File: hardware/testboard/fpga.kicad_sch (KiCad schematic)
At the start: 42 parts, among them J2 Conn_01x06, SW1 Button, U10 SN74ALVC164245, U11 ICE40HX4K-TQ144, U12 74AHCT04, U13 SST26VF023BA, U18 SN74LVC07, U19 SN74LVC07

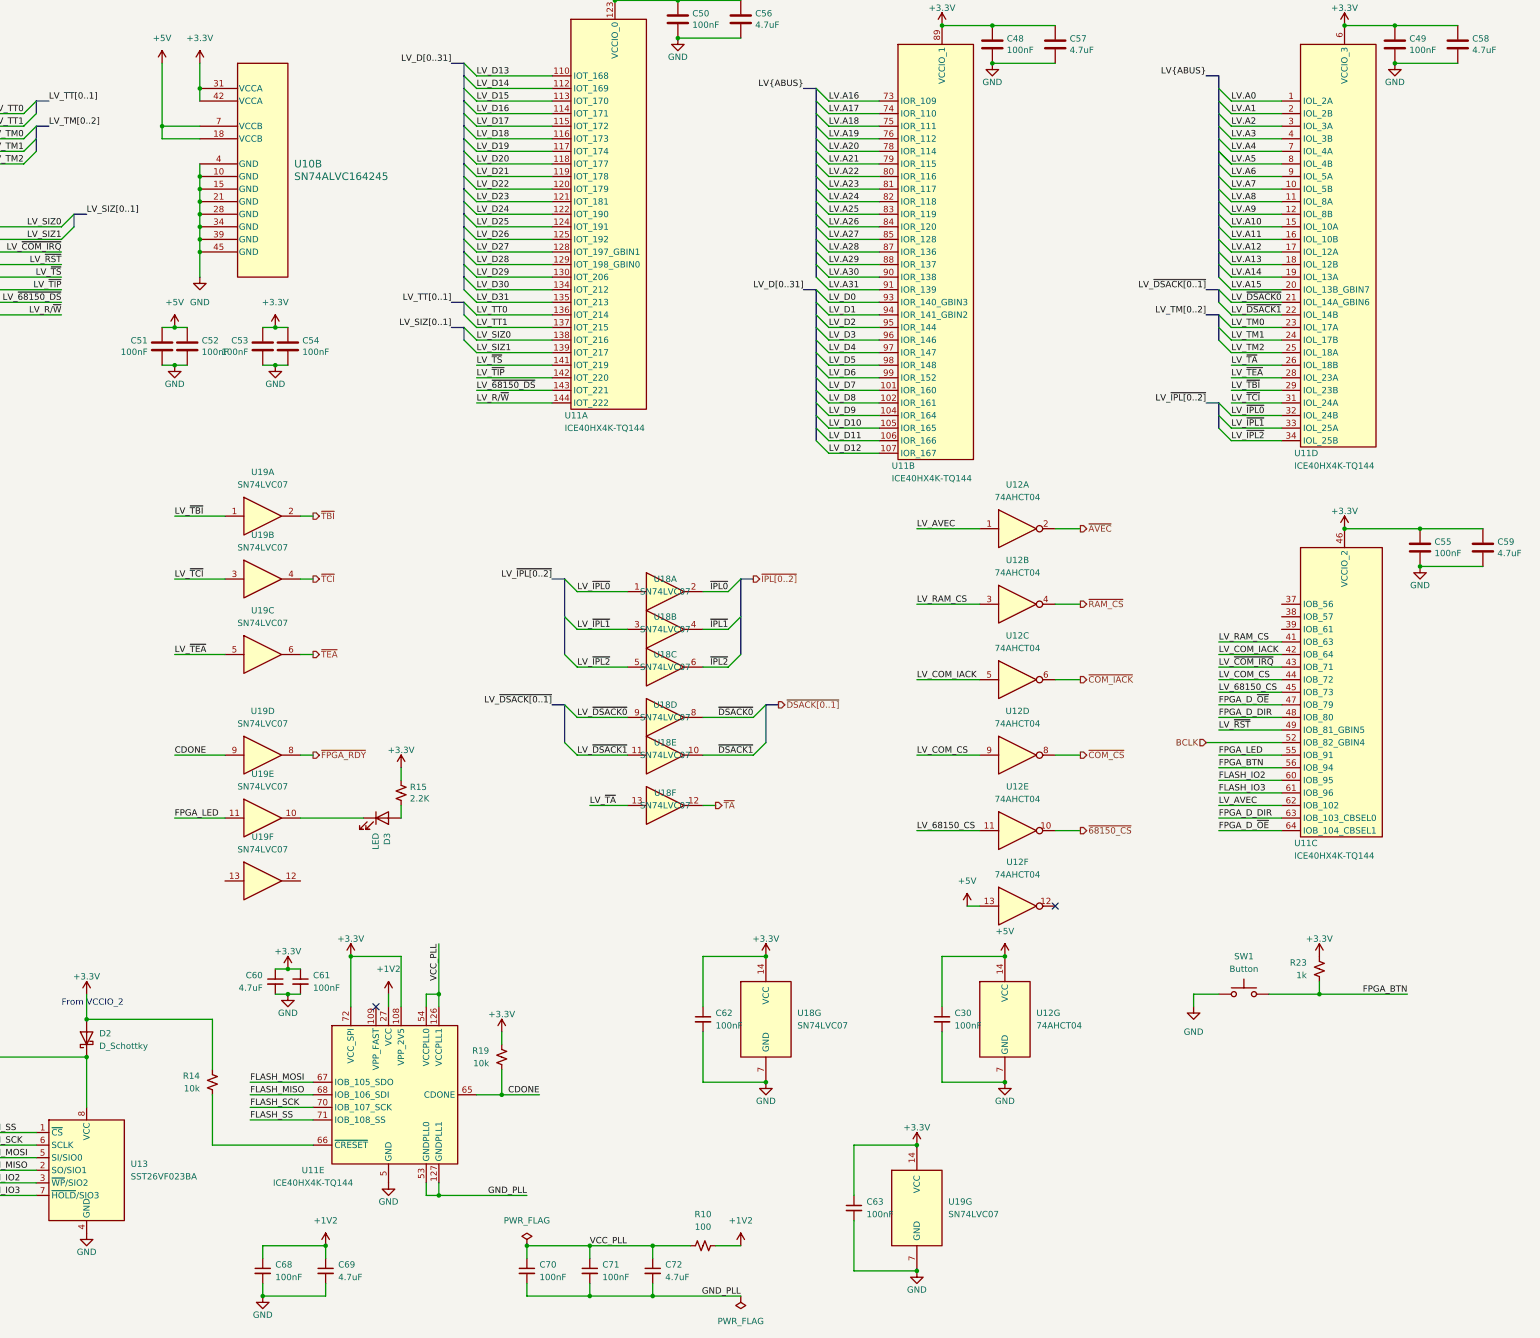
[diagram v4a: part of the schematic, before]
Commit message: fix up FPGA pinning
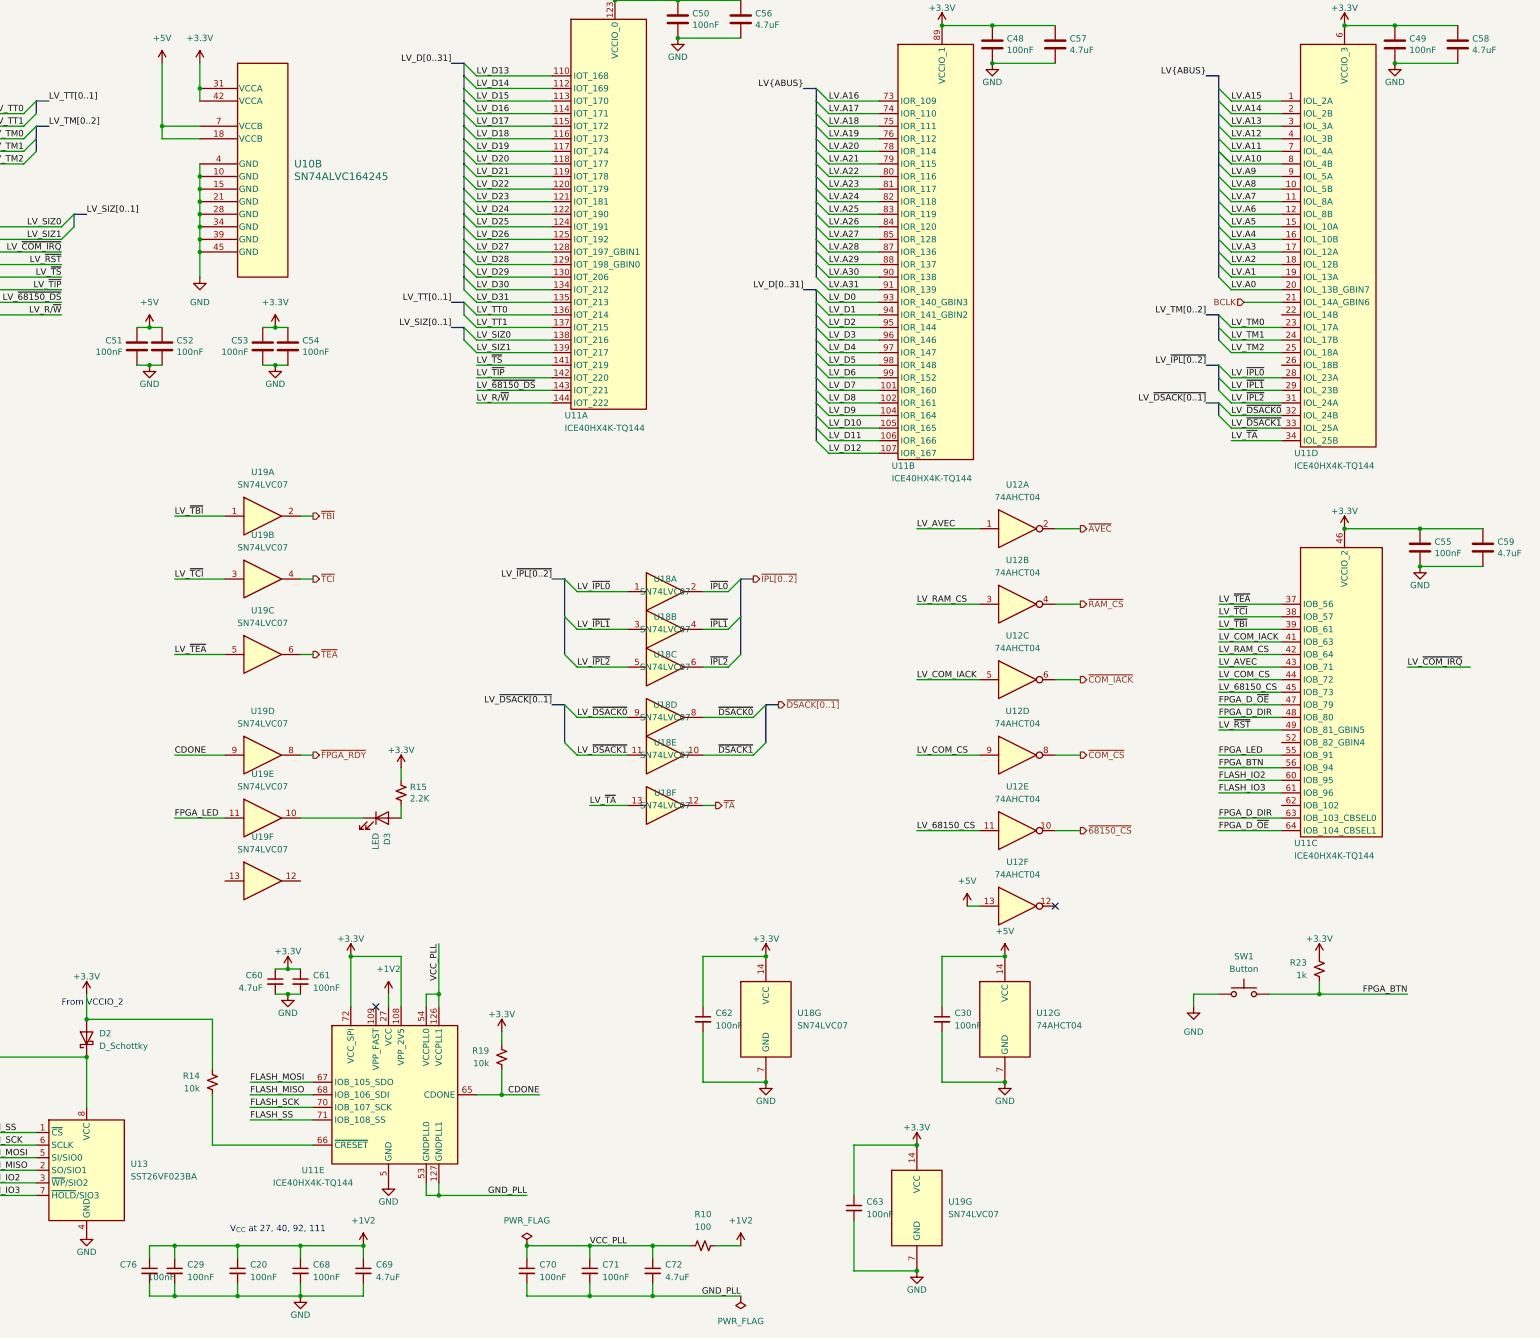
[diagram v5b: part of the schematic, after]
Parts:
- added C20, C29, C76: 100nF, Capacitor_SMD:C_0603_1608Metric, symbol Device:C_Small
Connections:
- net +1V2: now also C20.1, C29.1, C76.1
- net BCLK: now also U11.21 (IOL_14A_GBIN6); no longer U11.52 (IOB_82_GBIN4)
- net GND: now also C20.2, C29.2, C76.2
- net LV.A0: now also U11.20 (IOL_13B_GBIN7); no longer U11.1 (IOL_2A)
- net LV.A1: now also U11.19 (IOL_13A); no longer U11.2 (IOL_2B)
- net LV.A10: now also U11.8 (IOL_4B); no longer U11.15 (IOL_10A)
- net LV.A11: now also U11.7 (IOL_4A); no longer U11.16 (IOL_10B)
- net LV.A12: now also U11.4 (IOL_3B); no longer U11.17 (IOL_12A)
- net LV.A13: now also U11.3 (IOL_3A); no longer U11.18 (IOL_12B)
- net LV.A14: now also U11.2 (IOL_2B); no longer U11.19 (IOL_13A)
- net LV.A15: now also U11.1 (IOL_2A); no longer U11.20 (IOL_13B_GBIN7)
- net LV.A2: now also U11.18 (IOL_12B); no longer U11.3 (IOL_3A)
- net LV.A3: now also U11.17 (IOL_12A); no longer U11.4 (IOL_3B)
- net LV.A4: now also U11.16 (IOL_10B); no longer U11.7 (IOL_4A)
- net LV.A5: now also U11.15 (IOL_10A); no longer U11.8 (IOL_4B)
- net LV.A6: now also U11.12 (IOL_8B); no longer U11.9 (IOL_5A)
- net LV.A7: now also U11.11 (IOL_8A); no longer U11.10 (IOL_5B)
- net LV.A8: now also U11.10 (IOL_5B); no longer U11.11 (IOL_8A)
- net LV.A9: now also U11.9 (IOL_5A); no longer U11.12 (IOL_8B)
- net LV_AVEC: now also U11.43 (IOB_71); no longer U11.62 (IOB_102)
- net LV_COM_IACK: now also U11.41 (IOB_63); no longer U11.42 (IOB_64)
- net LV_RAM_CS: now also U11.42 (IOB_64); no longer U11.41 (IOB_63)
- net LV_~{COM_IRQ}: no longer U11.43 (IOB_71)
- net LV_~{DSACK0}: now also U11.32 (IOL_24B); no longer U11.21 (IOL_14A_GBIN6)
- net LV_~{DSACK1}: now also U11.33 (IOL_25A); no longer U11.22 (IOL_14B)
- net LV_~{IPL0}: now also U11.28 (IOL_23A); no longer U11.32 (IOL_24B)
- net LV_~{IPL1}: now also U11.29 (IOL_23B); no longer U11.33 (IOL_25A)
- net LV_~{IPL2}: now also U11.31 (IOL_24A); no longer U11.34 (IOL_25B)
- net LV_~{TA}: now also U11.34 (IOL_25B); no longer U11.26 (IOL_18B)
- net LV_~{TBI}: now also U11.39 (IOB_61); no longer U11.29 (IOL_23B)
- net LV_~{TCI}: now also U11.38 (IOB_57); no longer U11.31 (IOL_24A)
- net LV_~{TEA}: now also U11.37 (IOB_56); no longer U11.28 (IOL_23A)
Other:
- note added: "V_{CC} at 27, 40, 92, 111"
- moved on the sheet: C51, C52, C68, C69

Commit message: I ripped it all apart
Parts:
- added C? (x16): 100nF, Capacitor_SMD:C_0603_1608Metric, symbol Device:C
- added R?: R_Small_US, Resistor_SMD:R_0603_1608Metric, symbol Device:R_Small_US
- added U? (x8): SN74ALVC164245, Package_SO:TSSOP-48_6.1x12.5mm_P0.5mm, symbol 68040:SN74ALVC164245
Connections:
- net +3.3V: now also C?.1, C?.1, C?.1, C?.1, C?.1, C?.1, C?.1, C?.1, R?.1, U?.31 (VCCA), U?.31 (VCCA), U?.31 (VCCA), U?.31 (VCCA), U?.42 (VCCA), U?.42 (VCCA), U?.42 (VCCA), U?.42 (VCCA)
- net +5V: now also C?.1, C?.1, C?.1, C?.1, C?.1, C?.1, C?.1, C?.1, U?.18 (VCCB), U?.18 (VCCB), U?.18 (VCCB), U?.18 (VCCB), U?.7 (VCCB), U?.7 (VCCB), U?.7 (VCCB), U?.7 (VCCB)
- net BCLK: no longer U11.21 (IOL_14A_GBIN6)
- net FLASH_IO2: no longer U11.60 (IOB_95)
- net FLASH_IO3: no longer U11.61 (IOB_96)
- net FPGA_BTN: no longer U11.56 (IOB_94)
- net FPGA_D_DIR: no longer U11.48 (IOB_80), U11.63 (IOB_103_CBSEL0)
- net FPGA_D_~{OE}: no longer U11.47 (IOB_79), U11.64 (IOB_104_CBSEL1)
- net FPGA_LED: no longer U11.55 (IOB_91)
- net GND: now also C?.2, C?.2, C?.2, C?.2, C?.2, C?.2, C?.2, C?.2, C?.2, C?.2, C?.2, C?.2, C?.2, C?.2, C?.2, C?.2, U?.1 (1DIR), U?.1 (1DIR), U?.10 (GND), U?.10 (GND), U?.10 (GND), U?.10 (GND), U?.15 (GND), U?.15 (GND), U?.15 (GND), U?.15 (GND), U?.21 (GND), U?.21 (GND), U?.21 (GND), U?.21 (GND), U?.24 (2DIR), U?.24 (2DIR), U?.25 (*2OE), U?.25 (*2OE), U?.28 (GND), U?.28 (GND), U?.28 (GND), U?.28 (GND), U?.34 (GND), U?.34 (GND), U?.34 (GND), U?.34 (GND), U?.39 (GND), U?.39 (GND), U?.39 (GND), U?.39 (GND), U?.4 (GND), U?.4 (GND), U?.4 (GND), U?.4 (GND), U?.45 (GND), U?.45 (GND), U?.45 (GND), U?.45 (GND), U?.48 (*1OE), U?.48 (*1OE); no longer U10.11 (1B7), U10.12 (1B8), U10.9 (1B6)
- net LV.A0: now also U?.47 (1A1); no longer U11.20 (IOL_13B_GBIN7)
- net LV.A1: now also U?.46 (1A2); no longer U11.19 (IOL_13A)
- net LV.A10: now also U?.33 (2A3); no longer U11.8 (IOL_4B)
- net LV.A11: now also U?.32 (2A4); no longer U11.7 (IOL_4A)
- net LV.A12: now also U?.30 (2A5); no longer U11.4 (IOL_3B)
- net LV.A13: now also U?.29 (2A6); no longer U11.3 (IOL_3A)
- net LV.A14: now also U?.27 (2A7); no longer U11.2 (IOL_2B)
- net LV.A15: now also U?.26 (2A8); no longer U11.1 (IOL_2A)
- net LV.A16: now also U?.47 (1A1); no longer U11.73 (IOR_109)
- net LV.A17: now also U?.46 (1A2); no longer U11.74 (IOR_110)
- net LV.A18: now also U?.44 (1A3); no longer U11.75 (IOR_111)
- net LV.A19: now also U?.43 (1A4); no longer U11.76 (IOR_112)
- net LV.A2: now also U?.44 (1A3); no longer U11.18 (IOL_12B)
- net LV.A20: now also U?.41 (1A5); no longer U11.78 (IOR_114)
- net LV.A21: now also U?.40 (1A6); no longer U11.79 (IOR_115)
- net LV.A22: now also U?.38 (1A7); no longer U11.80 (IOR_116)
- net LV.A23: now also U?.37 (1A8); no longer U11.81 (IOR_117)
- net LV.A24: now also U?.36 (2A1); no longer U11.82 (IOR_118)
- net LV.A25: now also U?.35 (2A2); no longer U11.83 (IOR_119)
- net LV.A26: now also U?.33 (2A3); no longer U11.84 (IOR_120)
- net LV.A27: now also U?.32 (2A4); no longer U11.85 (IOR_128)
- net LV.A28: now also U?.30 (2A5); no longer U11.87 (IOR_136)
- net LV.A29: now also U?.29 (2A6); no longer U11.88 (IOR_137)
- net LV.A3: now also U?.43 (1A4); no longer U11.17 (IOL_12A)
- net LV.A30: now also U?.27 (2A7); no longer U11.90 (IOR_138)
- net LV.A31: now also U?.26 (2A8); no longer U11.91 (IOR_139)
- net LV.A4: now also U?.41 (1A5); no longer U11.16 (IOL_10B)
- net LV.A5: now also U?.40 (1A6); no longer U11.15 (IOL_10A)
- net LV.A6: now also U?.38 (1A7); no longer U11.12 (IOL_8B)
- net LV.A7: now also U?.37 (1A8); no longer U11.11 (IOL_8A)
- net LV.A8: now also U?.36 (2A1); no longer U11.10 (IOL_5B)
- net LV.A9: now also U?.35 (2A2); no longer U11.9 (IOL_5A)
- net LV_68150_CS: no longer U11.45 (IOB_73)
- net LV_AVEC: no longer U11.43 (IOB_71)
- net LV_COM_CS: no longer U11.44 (IOB_72)
- net LV_COM_IACK: no longer U11.41 (IOB_63)
- net LV_D0: now also U?.47 (1A1); no longer U11.93 (IOR_140_GBIN3)
- net LV_D1: now also U?.46 (1A2); no longer U11.94 (IOR_141_GBIN2)
- net LV_D10: now also U?.33 (2A3); no longer U11.105 (IOR_165)
- net LV_D11: now also U?.32 (2A4); no longer U11.106 (IOR_166)
- net LV_D12: now also U?.30 (2A5); no longer U11.107 (IOR_167)
- net LV_D13: now also U?.29 (2A6); no longer U11.110 (IOT_168)
- net LV_D14: now also U?.27 (2A7); no longer U11.112 (IOT_169)
- net LV_D15: now also U?.26 (2A8); no longer U11.113 (IOT_170)
- net LV_D16: now also U?.47 (1A1); no longer U11.114 (IOT_171)
- net LV_D17: now also U?.46 (1A2); no longer U11.115 (IOT_172)
- net LV_D18: now also U?.44 (1A3); no longer U11.116 (IOT_173)
- net LV_D19: now also U?.43 (1A4); no longer U11.117 (IOT_174)
- net LV_D2: now also U?.44 (1A3); no longer U11.95 (IOR_144)
- net LV_D20: now also U?.41 (1A5); no longer U11.118 (IOT_177)
- net LV_D21: now also U?.40 (1A6); no longer U11.119 (IOT_178)
- net LV_D22: now also U?.38 (1A7); no longer U11.120 (IOT_179)
- net LV_D23: now also U?.37 (1A8); no longer U11.121 (IOT_181)
- net LV_D24: now also U?.36 (2A1); no longer U11.122 (IOT_190)
- net LV_D25: now also U?.35 (2A2); no longer U11.124 (IOT_191)
- net LV_D26: now also U?.33 (2A3); no longer U11.125 (IOT_192)
- net LV_D27: now also U?.32 (2A4); no longer U11.128 (IOT_197_GBIN1)
- net LV_D28: now also U?.30 (2A5); no longer U11.129 (IOT_198_GBIN0)
- net LV_D29: now also U?.29 (2A6); no longer U11.130 (IOT_206)
- net LV_D3: now also U?.43 (1A4); no longer U11.96 (IOR_146)
- net LV_D30: now also U?.27 (2A7); no longer U11.134 (IOT_212)
- net LV_D31: now also U?.26 (2A8); no longer U11.135 (IOT_213)
- net LV_D4: now also U?.41 (1A5); no longer U11.97 (IOR_147)
- net LV_D5: now also U?.40 (1A6); no longer U11.98 (IOR_148)
- net LV_D6: now also U?.38 (1A7); no longer U11.99 (IOR_152)
- net LV_D7: now also U?.37 (1A8); no longer U11.101 (IOR_160)
- net LV_D8: now also U?.36 (2A1); no longer U11.102 (IOR_161)
- net LV_D9: now also U?.35 (2A2); no longer U11.104 (IOR_164)
- net LV_RAM_CS: no longer U11.42 (IOB_64)
- net LV_R/~{W}: no longer U10.26 (2A8), U11.144 (IOT_222)
- net LV_SIZ0: no longer U10.36 (2A1), U11.138 (IOT_216)
- net LV_SIZ1: no longer U10.35 (2A2), U11.139 (IOT_217)
- net LV_TM0: no longer U10.44 (1A3), U11.23 (IOL_17A)
- net LV_TM1: no longer U10.43 (1A4), U11.24 (IOL_17B)
- net LV_TM2: no longer U10.41 (1A5), U11.25 (IOL_18A)
- net LV_TT0: no longer U10.47 (1A1), U11.136 (IOT_214)
- net LV_TT1: no longer U10.46 (1A2), U11.137 (IOT_215)
- net LV_~{68150_DS}: no longer U10.27 (2A7), U11.143 (IOT_221)
- net LV_~{COM_IRQ}: no longer U10.33 (2A3)
- net LV_~{DSACK0}: no longer U11.32 (IOL_24B)
- net LV_~{DSACK1}: no longer U11.33 (IOL_25A)
- net LV_~{IPL0}: no longer U11.28 (IOL_23A)
- net LV_~{IPL1}: no longer U11.29 (IOL_23B)
- net LV_~{IPL2}: no longer U11.31 (IOL_24A)
- net LV_~{RST}: no longer U10.32 (2A4), U11.49 (IOB_81_GBIN5)
- net LV_~{TA}: no longer U11.34 (IOL_25B)
- net LV_~{TBI}: no longer U11.39 (IOB_61)
- net LV_~{TCI}: no longer U11.38 (IOB_57)
- net LV_~{TEA}: no longer U11.37 (IOB_56)
- net LV_~{TIP}: no longer U10.29 (2A6), U11.142 (IOT_220)
- net LV_~{TS}: no longer U10.30 (2A5), U11.141 (IOT_219)
- net R/~{W}: now also U10.13 (2B1); no longer U10.23 (2B8)
- net SIZ0: now also U10.12 (1B8); no longer U10.13 (2B1)
- net SIZ1: now also U10.11 (1B7); no longer U10.14 (2B2)
- net TM0: now also U10.9 (1B6); no longer U10.5 (1B3)
- net TM1: now also U10.8 (1B5); no longer U10.6 (1B4)
- net TM2: now also U10.6 (1B4); no longer U10.8 (1B5)
- net TT0: now also U10.5 (1B3); no longer U10.2 (1B1)
- net ~{68150_DS}: now also U10.2 (1B1); no longer U10.22 (2B7)
- net ~{RST}: now also U10.19 (2B5); no longer U10.17 (2B4)
- net ~{TS}: now also U10.22 (2B7); no longer U10.19 (2B5)
- new net A0: U?.2 (1B1)
- new net A1: U?.3 (1B2)
- new net A10: U?.16 (2B3)
- new net A11: U?.17 (2B4)
- new net A12: U?.19 (2B5)
- new net A13: U?.20 (2B6)
- new net A14: U?.22 (2B7)
- new net A15: U?.23 (2B8)
- new net A16: U?.2 (1B1)
- new net A17: U?.3 (1B2)
- new net A18: U?.5 (1B3)
- new net A19: U?.6 (1B4)
- new net A2: U?.5 (1B3)
- new net A20: U?.8 (1B5)
- new net A21: U?.9 (1B6)
- new net A22: U?.11 (1B7)
- new net A23: U?.12 (1B8)
- new net A24: U?.13 (2B1)
- new net A25: U?.14 (2B2)
- new net A26: U?.16 (2B3)
- new net A27: U?.17 (2B4)
- new net A28: U?.19 (2B5)
- new net A29: U?.20 (2B6)
- new net A3: U?.6 (1B4)
- new net A30: U?.22 (2B7)
- new net A31: U?.23 (2B8)
- new net A4: U?.8 (1B5)
- new net A5: U?.9 (1B6)
- new net A6: U?.11 (1B7)
- new net A7: U?.12 (1B8)
- new net A8: U?.13 (2B1)
- new net A9: U?.14 (2B2)
- new net D0: U?.2 (1B1)
- new net D1: U?.3 (1B2)
- new net D10: U?.16 (2B3)
- new net D11: U?.17 (2B4)
- new net D12: U?.19 (2B5)
- new net D13: U?.20 (2B6)
- new net D14: U?.22 (2B7)
- new net D15: U?.23 (2B8)
- new net D16: U?.2 (1B1)
- new net D17: U?.3 (1B2)
- new net D18: U?.5 (1B3)
- new net D19: U?.6 (1B4)
- new net D2: U?.5 (1B3)
- new net D20: U?.8 (1B5)
- new net D21: U?.9 (1B6)
- new net D22: U?.11 (1B7)
- new net D23: U?.12 (1B8)
- new net D24: U?.13 (2B1)
- new net D25: U?.14 (2B2)
- new net D26: U?.16 (2B3)
- new net D27: U?.17 (2B4)
- new net D28: U?.19 (2B5)
- new net D29: U?.20 (2B6)
- new net D3: U?.6 (1B4)
- new net D30: U?.22 (2B7)
- new net D31: U?.23 (2B8)
- new net D4: U?.8 (1B5)
- new net D5: U?.9 (1B6)
- new net D6: U?.11 (1B7)
- new net D7: U?.12 (1B8)
- new net D8: U?.13 (2B1)
- new net D9: U?.14 (2B2)
- new net FPGA_DBUF_DIR: U?.1 (1DIR), U?.1 (1DIR), U?.24 (2DIR), U?.24 (2DIR)
- new net FPGA_DBUF_~{OE}: R?.2, U?.25 (*2OE), U?.25 (*2OE), U?.48 (*1OE), U?.48 (*1OE)
- no-connect marks 5 -> 2
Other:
- removed sheet AddressBuffer
- removed sheet DataTRX
- moved on the sheet: C20, C29, C30, C31, C48, C49, C50, C51, C52, C53, C54, C55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

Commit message: pinouts
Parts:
- gave numbers to parts that had none: 21
- renumbered C31 to C801, C51 to C802, C52 to C803, C76 to C804, C53 to C805, C29 to C806, C54 to C807, C20 to C808, C60 to C809, C61 to C810, C68 to C811, C69 to C812, C70 to C813, C71 to C814, C72 to C815, C50 to C816, C56 to C821, C48 to C834, C57 to C835, C62 to C836, C30 to C837, C49 to C838, C58 to C839, C63 to C840, C55 to C841, C59 to C842, D1 to D801, D2 to D802, D3 to D803, J2 to J801, R16 to R801, R23 to R802, R17 to R803, R18 to R804, R14 to R805, R19 to R806, R10 to R808, R15 to R809, SW1 to SW801, U13 to U801, U10 to U802, U11 to U803, U18 to U808, U12 to U809, U19 to U810
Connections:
- net A0: now also U805.23 (2B8); no longer U806.2 (1B1)
- net A1: now also U805.22 (2B7); no longer U806.3 (1B2)
- net A10: now also U806.2 (1B1); no longer U806.16 (2B3)
- net A11: now also U806.3 (1B2); no longer U806.17 (2B4)
- net A12: now also U806.5 (1B3); no longer U806.19 (2B5)
- net A13: now also U806.6 (1B4); no longer U806.20 (2B6)
- net A14: now also U806.8 (1B5); no longer U806.22 (2B7)
- net A15: now also U806.11 (1B7); no longer U806.23 (2B8)
- net A16: now also U806.9 (1B6); no longer U807.2 (1B1)
- net A17: now also U806.12 (1B8); no longer U807.3 (1B2)
- net A18: now also U806.14 (2B2); no longer U807.5 (1B3)
- net A19: now also U806.13 (2B1); no longer U807.6 (1B4)
- net A2: now also U805.20 (2B6); no longer U806.5 (1B3)
- net A20: now also U806.17 (2B4); no longer U807.8 (1B5)
- net A21: now also U806.20 (2B6); no longer U807.9 (1B6)
- net A22: now also U807.12 (1B8); no longer U807.11 (1B7)
- net A23: now also U806.16 (2B3); no longer U807.12 (1B8)
- net A24: now also U807.8 (1B5); no longer U807.13 (2B1)
- net A25: now also U806.19 (2B5); no longer U807.14 (2B2)
- net A26: now also U807.11 (1B7); no longer U807.16 (2B3)
- net A27: now also U807.5 (1B3); no longer U807.17 (2B4)
- net A28: now also U807.9 (1B6); no longer U807.19 (2B5)
- net A29: now also U807.3 (1B2); no longer U807.20 (2B6)
- net A3: now also U805.19 (2B5); no longer U806.6 (1B4)
- net A30: now also U807.6 (1B4); no longer U807.22 (2B7)
- net A31: now also U807.2 (1B1); no longer U807.23 (2B8)
- net A4: now also U805.17 (2B4); no longer U806.8 (1B5)
- net A5: now also U805.16 (2B3); no longer U806.9 (1B6)
- net A6: now also U805.14 (2B2); no longer U806.11 (1B7)
- net A7: now also U805.13 (2B1); no longer U806.12 (1B8)
- net A8: now also U806.23 (2B8); no longer U806.13 (2B1)
- net A9: now also U806.22 (2B7); no longer U806.14 (2B2)
- net BCLK: now also U803.94 (IOR_141_GBIN2)
- net D0: now also U807.13 (2B1); no longer U804.2 (1B1)
- net D1: now also U807.14 (2B2); no longer U804.3 (1B2)
- net D10: now also U804.5 (1B3); no longer U804.16 (2B3)
- net D11: now also U804.6 (1B4); no longer U804.17 (2B4)
- net D12: now also U804.8 (1B5); no longer U804.19 (2B5)
- net D13: now also U804.11 (1B7); no longer U804.20 (2B6)
- net D14: now also U804.13 (2B1); no longer U804.22 (2B7)
- net D15: now also U804.14 (2B2); no longer U804.23 (2B8)
- net D16: now also U804.9 (1B6); no longer U805.2 (1B1)
- net D17: now also U804.16 (2B3); no longer U805.3 (1B2)
- net D18: now also U804.12 (1B8); no longer U805.5 (1B3)
- net D19: now also U804.19 (2B5); no longer U805.6 (1B4)
- net D2: now also U807.17 (2B4); no longer U804.5 (1B3)
- net D20: now also U804.22 (2B7); no longer U805.8 (1B5)
- net D21: now also U805.2 (1B1); no longer U805.9 (1B6)
- net D22: now also U804.20 (2B6); no longer U805.11 (1B7)
- net D23: now also U804.17 (2B4); no longer U805.12 (1B8)
- net D24: now also U805.3 (1B2); no longer U805.13 (2B1)
- net D25: now also U804.23 (2B8); no longer U805.14 (2B2)
- net D26: now also U805.5 (1B3); no longer U805.16 (2B3)
- net D27: now also U805.8 (1B5); no longer U805.17 (2B4)
- net D28: now also U805.6 (1B4); no longer U805.19 (2B5)
- net D29: now also U805.11 (1B7); no longer U805.20 (2B6)
- net D3: now also U807.16 (2B3); no longer U804.6 (1B4)
- net D30: now also U805.12 (1B8); no longer U805.22 (2B7)
- net D31: now also U805.9 (1B6); no longer U805.23 (2B8)
- net D4: now also U807.19 (2B5); no longer U804.8 (1B5)
- net D5: now also U807.20 (2B6); no longer U804.9 (1B6)
- net D6: now also U807.22 (2B7); no longer U804.11 (1B7)
- net D7: now also U807.23 (2B8); no longer U804.12 (1B8)
- net D8: now also U804.2 (1B1); no longer U804.13 (2B1)
- net D9: now also U804.3 (1B2); no longer U804.14 (2B2)
- net FLASH_IO2: now also U803.56 (IOB_94)
- net FLASH_IO3: now also U803.60 (IOB_95)
- net FPGA_BTN: now also U803.55 (IOB_91)
- net FPGA_DBUF_DIR: no longer U805.24 (2DIR)
- net FPGA_DBUF_~{OE}: no longer U805.25 (*2OE)
- net FPGA_D_DIR: now also U803.47 (IOB_79), U803.62 (IOB_102)
- net FPGA_D_~{OE}: now also U803.45 (IOB_73), U803.63 (IOB_103_CBSEL0)
- net FPGA_LED: now also U803.52 (IOB_82_GBIN4)
- net GND: no longer U807.24 (2DIR), U807.25 (*2OE)
- net LV.A0: now also U803.37 (IOB_56), U805.26 (2A8); no longer U806.47 (1A1)
- net LV.A1: now also U803.34 (IOL_25B), U805.27 (2A7); no longer U806.46 (1A2)
- net LV.A10: now also U803.23 (IOL_17A), U806.47 (1A1); no longer U806.33 (2A3)
- net LV.A11: now also U803.22 (IOL_14B), U806.46 (1A2); no longer U806.32 (2A4)
- net LV.A12: now also U803.21 (IOL_14A_GBIN6), U806.44 (1A3); no longer U806.30 (2A5)
- net LV.A13: now also U803.20 (IOL_13B_GBIN7), U806.43 (1A4); no longer U806.29 (2A6)
- net LV.A14: now also U803.19 (IOL_13A), U806.41 (1A5); no longer U806.27 (2A7)
- net LV.A15: now also U803.18 (IOL_12B), U806.38 (1A7); no longer U806.26 (2A8)
- net LV.A16: now also U803.73 (IOR_109), U806.40 (1A6); no longer U807.47 (1A1)
- net LV.A17: now also U803.74 (IOR_110), U806.37 (1A8); no longer U807.46 (1A2)
- net LV.A18: now also U803.75 (IOR_111), U806.35 (2A2); no longer U807.44 (1A3)
- net LV.A19: now also U803.76 (IOR_112), U806.36 (2A1); no longer U807.43 (1A4)
- net LV.A2: now also U803.33 (IOL_25A), U805.29 (2A6); no longer U806.44 (1A3)
- net LV.A20: now also U803.78 (IOR_114), U806.32 (2A4); no longer U807.41 (1A5)
- net LV.A21: now also U803.79 (IOR_115), U806.29 (2A6); no longer U807.40 (1A6)
- net LV.A22: now also U803.80 (IOR_116), U807.37 (1A8); no longer U807.38 (1A7)
- net LV.A23: now also U803.81 (IOR_117), U806.33 (2A3); no longer U807.37 (1A8)
- net LV.A24: now also U803.82 (IOR_118), U807.41 (1A5); no longer U807.36 (2A1)
- net LV.A25: now also U803.83 (IOR_119), U806.30 (2A5); no longer U807.35 (2A2)
- net LV.A26: now also U803.84 (IOR_120), U807.38 (1A7); no longer U807.33 (2A3)
- net LV.A27: now also U803.85 (IOR_128), U807.44 (1A3); no longer U807.32 (2A4)
- net LV.A28: now also U803.87 (IOR_136), U807.40 (1A6); no longer U807.30 (2A5)
- net LV.A29: now also U803.88 (IOR_137), U807.46 (1A2); no longer U807.29 (2A6)
- net LV.A3: now also U803.32 (IOL_24B), U805.30 (2A5); no longer U806.43 (1A4)
- net LV.A30: now also U803.90 (IOR_138), U807.43 (1A4); no longer U807.27 (2A7)
- net LV.A31: now also U803.91 (IOR_139), U807.47 (1A1); no longer U807.26 (2A8)
- net LV.A4: now also U803.31 (IOL_24A), U805.32 (2A4); no longer U806.41 (1A5)
- net LV.A5: now also U803.29 (IOL_23B), U805.33 (2A3); no longer U806.40 (1A6)
- net LV.A6: now also U803.28 (IOL_23A), U805.35 (2A2); no longer U806.38 (1A7)
- net LV.A7: now also U803.26 (IOL_18B), U805.36 (2A1); no longer U806.37 (1A8)
- net LV.A8: now also U803.25 (IOL_18A), U806.26 (2A8); no longer U806.36 (2A1)
- net LV.A9: now also U803.24 (IOL_17B), U806.27 (2A7); no longer U806.35 (2A2)
- net LV_68150_CS: now also U803.44 (IOB_72)
- net LV_AVEC: now also U803.42 (IOB_64)
- net LV_COM_CS: now also U803.43 (IOB_71)
- net LV_COM_IACK: now also U803.39 (IOB_61)
- net LV_D0: now also U803.102 (IOR_161), U807.36 (2A1)
- net LV_D1: now also U803.104 (IOR_164), U807.35 (2A2)
- net LV_D10: now also U803.116 (IOT_173)
- net LV_D11: now also U803.117 (IOT_174)
- net LV_D12: now also U803.118 (IOT_177)
- net LV_D13: now also U803.119 (IOT_178)
- net LV_D14: now also U803.120 (IOT_179)
- net LV_D15: now also U803.121 (IOT_181)
- net LV_D16: now also U803.1 (IOL_2A)
- net LV_D17: now also U803.144 (IOT_222)
- net LV_D18: now also U803.143 (IOT_221)
- net LV_D19: now also U803.142 (IOT_220)
- net LV_D2: now also U803.105 (IOR_165), U807.32 (2A4)
- net LV_D20: now also U803.141 (IOT_219)
- net LV_D21: now also U803.139 (IOT_217)
- net LV_D22: now also U803.138 (IOT_216)
- net LV_D23: now also U803.137 (IOT_215)
- net LV_D24: now also U803.136 (IOT_214); no longer U805.36 (2A1)
- net LV_D25: now also U803.135 (IOT_213); no longer U805.35 (2A2)
- net LV_D26: now also U803.134 (IOT_212); no longer U805.33 (2A3)
- net LV_D27: now also U803.130 (IOT_206); no longer U805.32 (2A4)
- net LV_D28: now also U803.129 (IOT_198_GBIN0); no longer U805.30 (2A5)
- net LV_D29: now also U803.128 (IOT_197_GBIN1); no longer U805.29 (2A6)
- net LV_D3: now also U803.106 (IOR_166), U807.33 (2A3)
- net LV_D30: now also U803.125 (IOT_192); no longer U805.27 (2A7)
- net LV_D31: now also U803.124 (IOT_191); no longer U805.26 (2A8)
- net LV_D4: now also U803.107 (IOR_167), U807.30 (2A5)
- net LV_D5: now also U803.110 (IOT_168), U807.29 (2A6)
- net LV_D6: now also U803.112 (IOT_169), U807.27 (2A7)
- net LV_D7: now also U803.113 (IOT_170), U807.26 (2A8)
- net LV_D8: now also U803.114 (IOT_171)
- net LV_D9: now also U803.115 (IOT_172)
- net LV_RAM_CS: now also U803.41 (IOB_63)
- net LV_R/~{W}: now also U802.43 (1A4), U803.122 (IOT_190)
- net LV_SIZ0: now also U802.41 (1A5), U803.96 (IOR_146)
- net LV_SIZ1: now also U802.40 (1A6), U803.97 (IOR_147)
- net LV_TM0: now also U802.44 (1A3), U803.8 (IOL_4B)
- net LV_TM1: now also U802.46 (1A2), U803.9 (IOL_5A)
- net LV_TM2: now also U802.47 (1A1), U803.10 (IOL_5B)
- net LV_TT0: now also U803.93 (IOR_140_GBIN3)
- net LV_TT1: now also U803.95 (IOR_144)
- net LV_~{68150_DS}: now also U803.101 (IOR_160)
- net LV_~{COM_IRQ}: now also U803.64 (IOB_104_CBSEL1)
- net LV_~{DSACK0}: now also U803.11 (IOL_8A)
- net LV_~{DSACK1}: now also U803.12 (IOL_8B)
- net LV_~{IPL0}: now also U803.2 (IOL_2B)
- net LV_~{IPL1}: now also U803.3 (IOL_3A)
- net LV_~{IPL2}: now also U803.4 (IOL_3B)
- net LV_~{RST}: now also U803.48 (IOB_80)
- net LV_~{TA}: now also U803.7 (IOL_4A)
- net LV_~{TBI}: now also U803.17 (IOL_12A)
- net LV_~{TCI}: now also U803.16 (IOL_10B)
- net LV_~{TEA}: now also U803.15 (IOL_10A)
- net LV_~{TIP}: now also U802.37 (1A8), U803.99 (IOR_152)
- net LV_~{TS}: now also U802.38 (1A7), U803.98 (IOR_148)
- net R/~{W}: now also U802.6 (1B4); no longer U802.13 (2B1)
- net SIZ0: now also U802.8 (1B5); no longer U802.12 (1B8)
- net SIZ1: now also U802.9 (1B6); no longer U802.11 (1B7)
- net TM0: now also U802.5 (1B3); no longer U802.9 (1B6)
- net TM1: now also U802.3 (1B2); no longer U802.8 (1B5)
- net TM2: now also U802.2 (1B1); no longer U802.6 (1B4)
- net TT0: no longer U802.5 (1B3)
- net TT1: no longer U802.3 (1B2)
- net ~{68150_DS}: no longer U802.2 (1B1)
- net ~{TIP}: now also U802.12 (1B8); no longer U802.20 (2B6)
- net ~{TS}: now also U802.11 (1B7); no longer U802.22 (2B7)
